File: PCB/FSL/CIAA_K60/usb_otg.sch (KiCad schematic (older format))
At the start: 13 parts, among them J502 USB OTG, U501 MIC2025-2YM, U502 PRTR5V0U2X

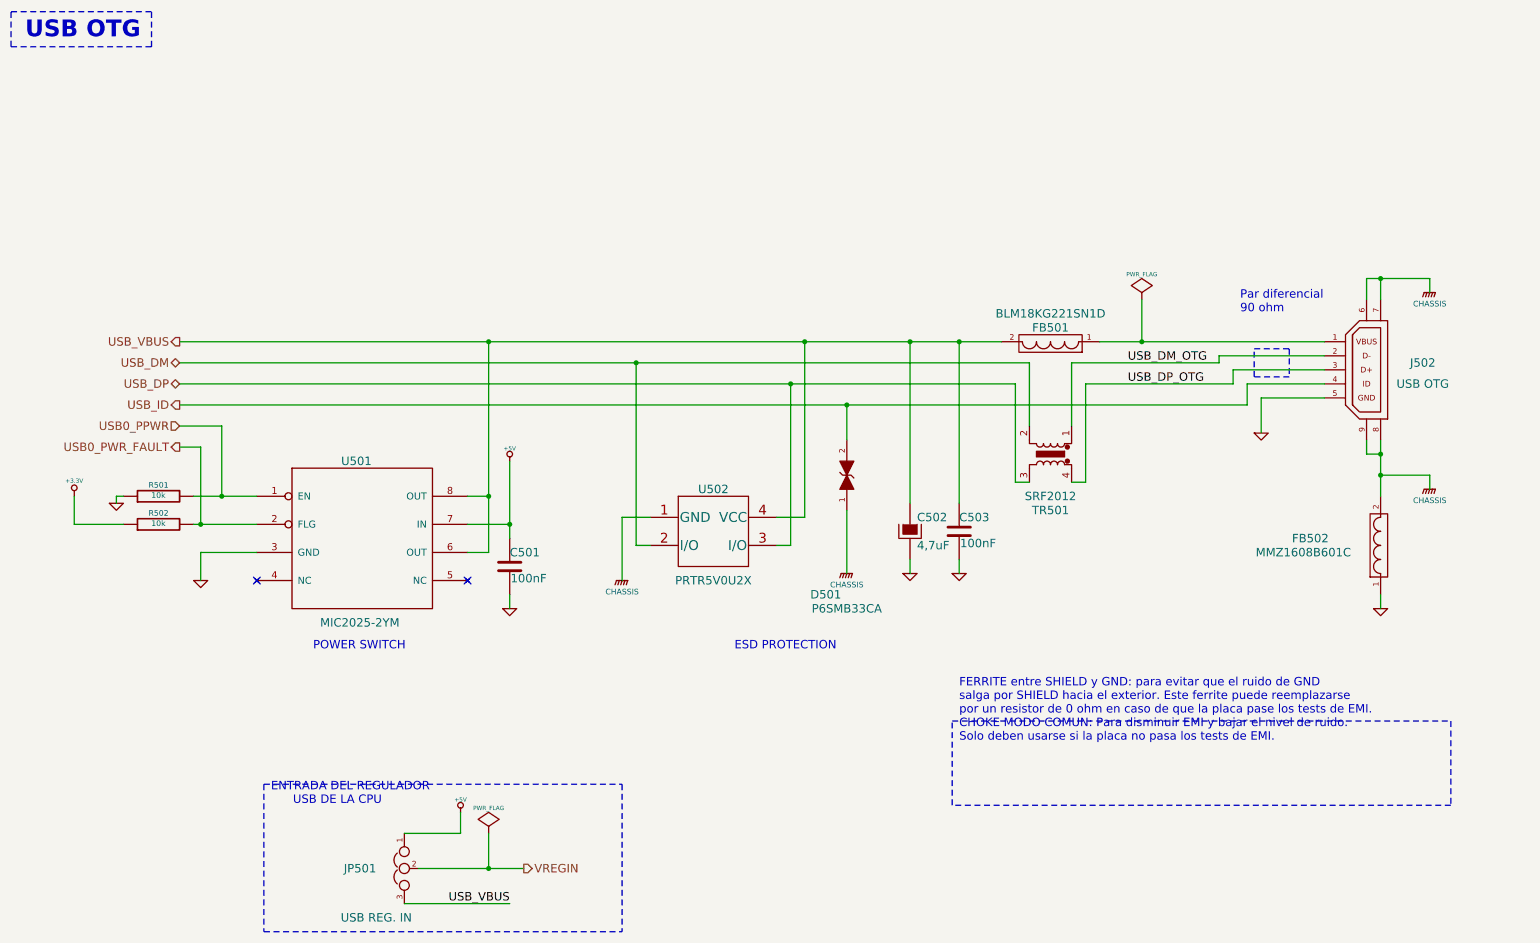
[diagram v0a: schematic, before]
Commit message: Actualizacion de esquematicos. Circuito impreso y modelos 3D
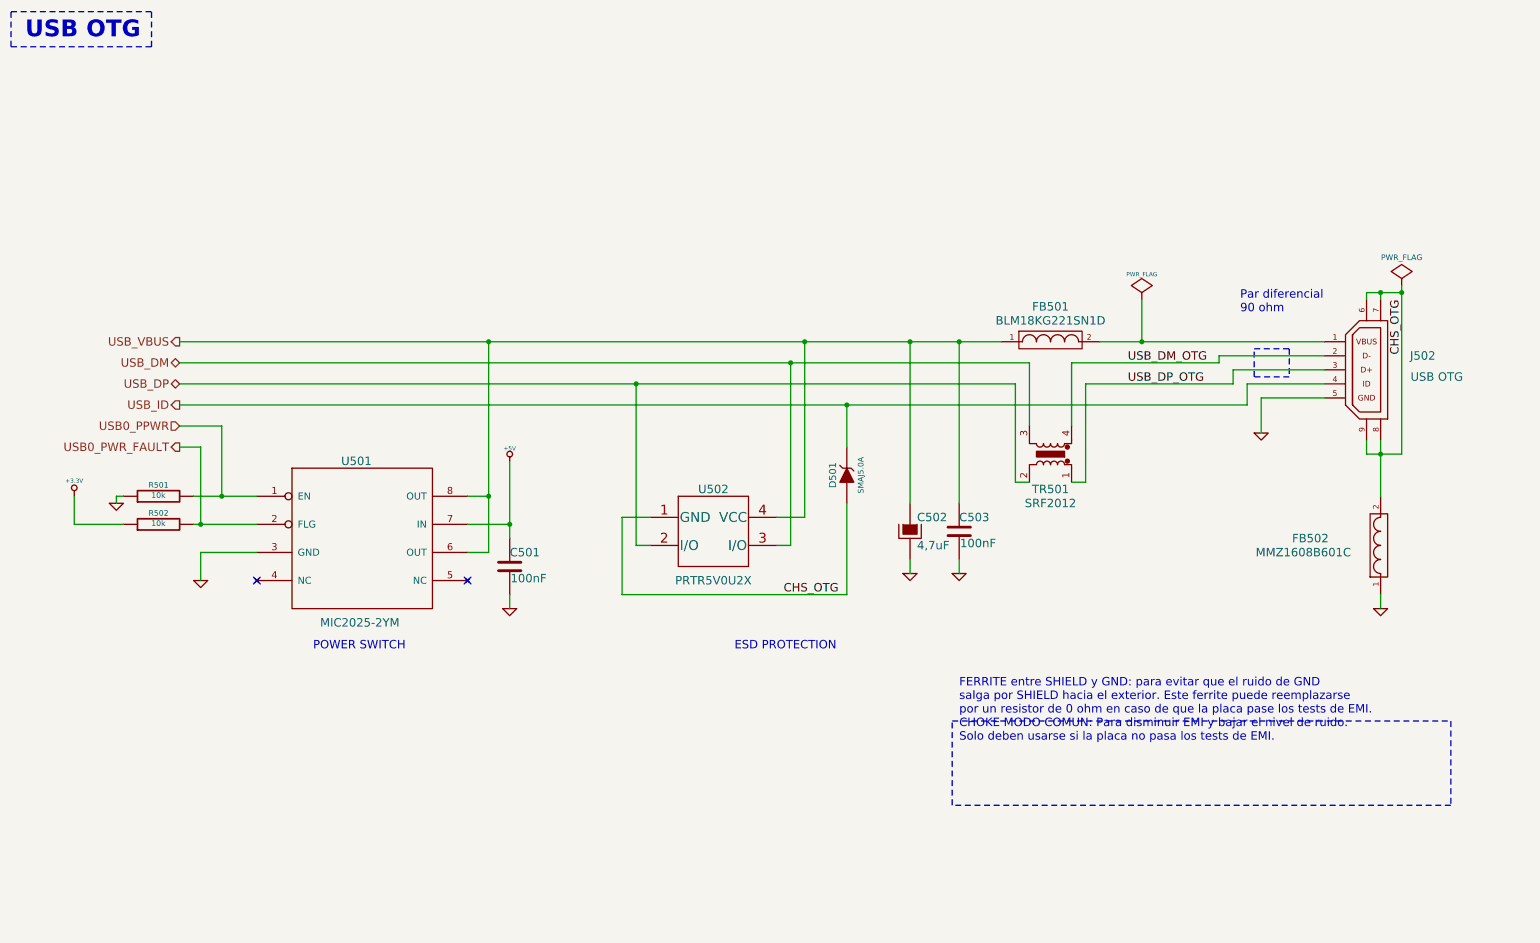
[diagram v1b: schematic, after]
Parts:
- removed D501: P6SMB33CA, DO-214AA_SMB, symbol TVS
- removed JP501: USB REG. IN, PIN_ARRAY_3x1, symbol JUMPER3
- added D501: SMAJ5.0A, DO-214AC_SMA, symbol ZENER
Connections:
- net USB_DM: now also TR501.3, U502.3 (I/O); no longer TR501.2, U502.2 (I/O)
- net USB_DM_OTG: now also TR501.4; no longer TR501.1
- net USB_DP: now also TR501.2, U502.2 (I/O); no longer TR501.3, U502.3 (I/O)
- net USB_DP_OTG: now also TR501.1; no longer TR501.4
- net USB_ID: now also D501.2 (K)
- net USB_VBUS: now also FB501.1; no longer FB501.2
- net at J502.1 (VBUS): now also FB501.2; no longer FB501.1
- net GNDPWR renamed CHS_OTG
- net CHS_OTG: now also D501.1 (A)
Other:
- note removed: "ENTRADA DEL REGULADOR\n USB DE LA CPU"

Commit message: Actualizacion de Licencia y avances
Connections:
- net USB_DM: now also U502.2 (I/O); no longer U502.3 (I/O)
- net USB_DP: now also U502.3 (I/O); no longer U502.2 (I/O)
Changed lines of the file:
@@
 Sheet 5 13
 Title "USB OTG"
-Date "24 jul 2014"
+Date "1 aug 2014"
 Rev "1.0"
 Comp "CIAA - COMPUTADORA INDUSTRIAL ABIERTA ARGENTINA. Versión FSL (Freescale K60)"
@@
 	6500 4700 4900 4700
 Wire Wire Line
-	5000 4350 5000 3200
-Connection ~ 5000 3200
-Wire Wire Line
-	6100 4350 6100 3050
-Connection ~ 6100 3050
+	6100 4350 6100 3200
+Connection ~ 6100 3200
+Wire Wire Line
+	5000 4350 5000 3050
+Connection ~ 5000 3050
 $EndSCHEMATC

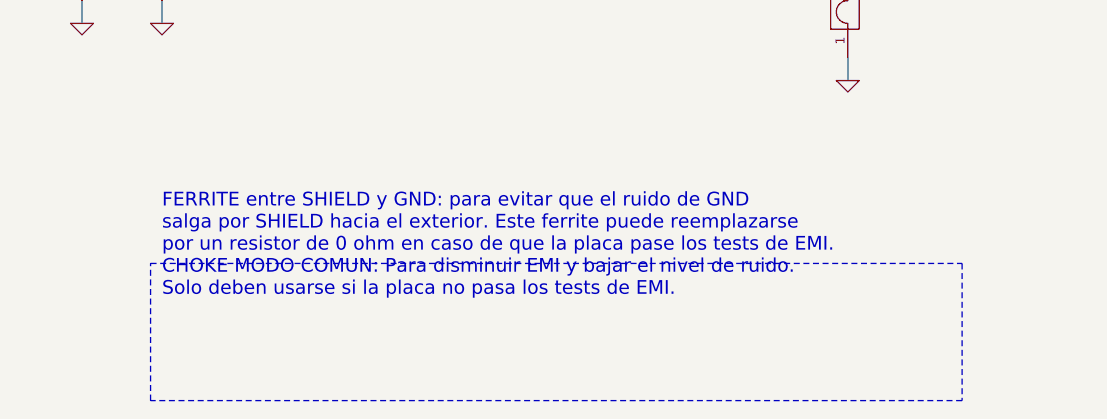
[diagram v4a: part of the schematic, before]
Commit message: Sch files adapted to new eeschema. Fixing some text locations.
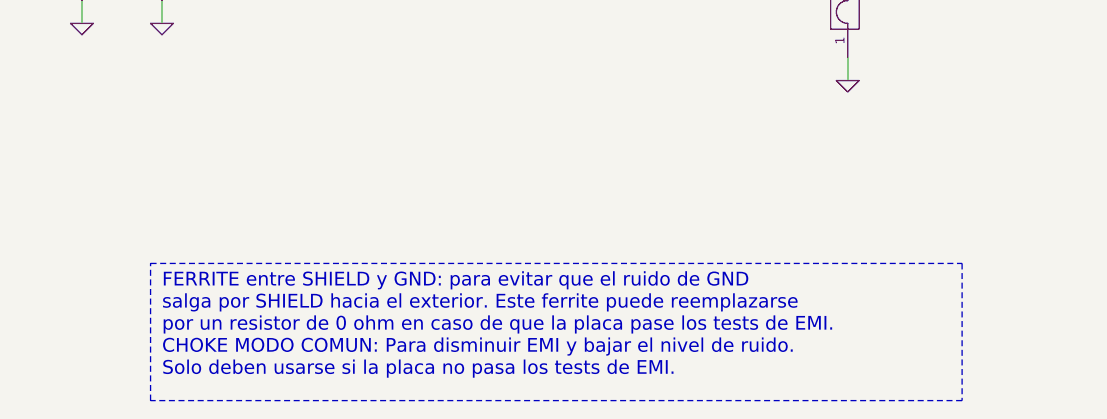
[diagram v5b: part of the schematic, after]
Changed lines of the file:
@@
 EESchema Schematic File Version 2
 LIBS:CIAAK60LIB
-EELAYER 27 0
+LIBS:CIAA_K60-cache
+EELAYER 25 0
 EELAYER END
 $Descr A4 11693 8268
@@
 Text Notes 9300 2700 0    60   ~ 0
 Par diferencial \n90 ohm
-Text Notes 7300 5750 0    60   ~ 0
+Text Notes 7300 6100 0    60   ~ 0
 FERRITE entre SHIELD y GND: para evitar que el ruido de GND\nsalga por SHIELD hacia el exterior. Este ferrite puede reemplazarse \npor un resistor de 0 ohm en caso de que la placa pase los tests de EMI. \nCHOKE MODO COMUN: Para disminuir EMI y bajar el nivel de ruido. \nSolo deben usarse si la placa no pasa los tests de EMI.
 Text Notes 2700 5100 0    60   ~ 0

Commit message: Renaming symbol field-names in .sch files for KiCost integration.
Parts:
- C501, C503: Desc (none) -> CAP CER 0,1UF 16V X7R 10% 0603; Descripcion CAP CER 0,1UF 16V X7R 10% 0603 -> (none); Digikey# (none) -> 399-1096-1-ND; Digikey/Mouser 399-1096-1-ND -> (none); Fabricante KEMET -> (none); Manf (none) -> Kemet; Manf# (none) -> C0603C104K4RACTU; Nro. parte C0603C104K4RACTU -> (none)
- C502: Desc (none) -> CAP TANT 4,7uF 6,3V 10% 1206; Descripcion CAP TANT 4,7uF 6,3V 10% 1206 -> (none); Digikey# (none) -> 399-9717-1-ND; Digikey/Mouser 399-9717-1-ND -> (none); Fabricante KEMET -> (none); Manf (none) -> Kemet; Manf# (none) -> T491A475K006AT; Nro. parte T491A475K006AT -> (none)
- D501: Desc (none) -> TVS DIODE 5VWM SMD; Descripcion TVS DIODE 5VWM SMD -> (none); Digikey# (none) -> SMAJ5.0ABCT-ND; Digikey/Mouser SMAJ5.0ABCT-ND -> (none); Fabricante Bourns Inc. -> (none); Manf (none) -> Bourns; Manf# (none) -> SMAJ5.0A; Nro. parte SMAJ5.0A -> (none)
- FB501: Desc (none) -> FERRITE CHIP 220 OHM 2200MA 0603; Descripcion FERRITE CHIP 220 OHM 2200MA 0603 -> (none); Digikey# (none) -> 490-5255-1-ND; Digikey/Mouser 490-5255-1-ND -> (none); Fabricante MURATA -> (none); Manf (none) -> MURATA; Manf# (none) -> BLM18KG221SN1D; Nro. parte BLM18KG221SN1D -> (none)
- FB502: Desc (none) -> FERRITE CHIP 600 OHM 500MA 0603; Descripcion FERRITE CHIP 600 OHM 500MA 0603 -> (none); Digikey# (none) -> 445-2166-1-ND; Digikey/Mouser 445-2166-1-ND -> (none); Fabricante TDK -> (none); Manf (none) -> TDK; Manf# (none) -> MMZ1608B601C; Nro. parte MMZ1608B601C -> (none)
- J502: Desc (none) -> CONNECTOR RECEPTACLE MICRO USB AB SMD BOTTOM MOUNT; Descripcion CONNECTOR RECEPTACLE MICRO USB AB SMD BOTTOM MOUNT -> (none); Digikey# (none) -> H11635TR-ND; Digikey/Mouser H11635TR-ND -> (none); Fabricante HIROSE ELECTRIC -> (none); Manf (none) -> HIROSE ELECTRIC; Manf# (none) -> ZX62-AB-5PA(11); Nro. parte ZX62-AB-5PA(11) -> (none)
- R501, R502: Desc (none) -> RESISTOR 10k 1/10W 5% 0603; Descripcion RESISTOR 10k 1/10W 5% 0603 -> (none); Digikey# (none) -> 311-10KGRCT-ND; Digikey/Mouser 311-10KGRCT-ND -> (none); Fabricante YAGEO -> (none); Manf (none) -> Yageo; Manf# (none) -> RC0603JR-0710KL; Nro. parte RC0603JR-0710KL -> (none)
- TR501: Desc (none) -> INDUCTOR COMMON MODE 90 OHM SMD; Descripcion INDUCTOR COMMON MODE 90 OHM SMD -> (none); Digikey# (none) -> SRF2012-900YCT-ND; Digikey/Mouser SRF2012-900YCT-ND -> (none); Fabricante BOURNS -> (none); Manf (none) -> BOURNS; Manf# (none) -> SRF2012-900Y; Nro. parte SRF2012-900Y -> (none)
- U501: Desc (none) -> IC SINGLE CHANNEL POWER DISTRIBUTION SWITCH 500mA; Descripcion IC SINGLE CHANNEL POWER DISTRIBUTION SWITCH 500mA -> (none); Digikey# (none) -> 576-1058-ND; Digikey/Mouser 576-1058-ND -> (none); Fabricante MICREL -> (none); Manf (none) -> MICREL; Manf# (none) -> MIC2025-2YM; Nro. parte MIC2025-2YM -> (none)
- U502: Desc (none) -> IC TVS DIODE 2 CHANNEL 10V CLAMP SOT1434; Descripcion IC TVS DIODE 2 CHANNEL 10V CLAMP SOT1434 -> (none); Digikey# (none) -> CM1213A-02SROSCT-ND; Digikey/Mouser CM1213A-02SROSCT-ND -> (none); Fabricante ON SEMICONDUCTOR -> (none); Manf (none) -> ON SEMICONDUCTOR; Manf# (none) -> CM1213A-02SR; Nro. parte CM1213A-02SR -> (none)
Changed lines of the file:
@@
 F 2 "SOIC-8" H 3050 4300 60  0001 C CNN
 F 3 "~" H 3050 4300 60  0000 C CNN
-F 4 "IC SINGLE CHANNEL POWER DISTRIBUTION SWITCH 500mA" H 3050 4300 60  0001 C CNN "Descripcion"
-F 5 "MICREL" H 3050 4300 60  0001 C CNN "Fabricante"
-F 6 "MIC2025-2YM" H 3050 4300 60  0001 C CNN "Nro. parte"
+F 4 "IC SINGLE CHANNEL POWER DISTRIBUTION SWITCH 500mA" H 3050 4300 60  0001 C CNN "Desc"
+F 5 "MICREL" H 3050 4300 60  0001 C CNN "Manf"
+F 6 "MIC2025-2YM" H 3050 4300 60  0001 C CNN "Manf#"
 F 7 "../datasheets/ic/mic2025.pdf" H 3050 4300 60  0001 C CNN "Path datasheet"
-F 8 "576-1058-ND" H 3050 4300 60  0001 C CNN "Digikey/Mouser"
+F 8 "576-1058-ND" H 3050 4300 60  0001 C CNN "Digikey#"
 F 9 "SOIC-8" H 3050 4300 60  0001 C CNN "Footprint estandar"
 	1    3050 4300
@@
 F 2 "SOT-143-4" H 7100 3600 60  0001 C CNN
 F 3 "~" H 7100 3600 60  0000 C CNN
-F 4 "IC TVS DIODE 2 CHANNEL 10V CLAMP SOT1434" H 5550 4250 60  0001 C CNN "Descripcion"
-F 5 "ON SEMICONDUCTOR" H 5550 4250 60  0001 C CNN "Fabricante"
-F 6 "CM1213A-02SR" H 5550 4250 60  0001 C CNN "Nro. parte"
+F 4 "IC TVS DIODE 2 CHANNEL 10V CLAMP SOT1434" H 5550 4250 60  0001 C CNN "Desc"
+F 5 "ON SEMICONDUCTOR" H 5550 4250 60  0001 C CNN "Manf"
+F 6 "CM1213A-02SR" H 5550 4250 60  0001 C CNN "Manf#"
 F 7 "../datasheets/passive/protect/CM1213A-D.PDF" H 5550 4250 60  0001 C CNN "Path datasheet"
-F 8 "CM1213A-02SROSCT-ND" H 5550 4250 60  0001 C CNN "Digikey/Mouser"
+F 8 "CM1213A-02SROSCT-ND" H 5550 4250 60  0001 C CNN "Digikey#"
 F 9 "SOT-143-4" H 5550 4250 60  0001 C CNN "Footprint estandar"
 	1    5550 4250
@@
 F 2 "c_1206POL" H 7050 4100 30  0001 C CNN
 F 3 "~" H 6950 4250 300 0000 C CNN
-F 4 "CAP TANT 4,7uF 6,3V 10% 1206 " H 6950 4250 60  0001 C CNN "Descripcion"
-F 5 "KEMET" H 6950 4250 60  0001 C CNN "Fabricante"
-F 6 "T491A475K006AT" H 6950 4250 60  0001 C CNN "Nro. parte"
+F 4 "CAP TANT 4,7uF 6,3V 10% 1206 " H 6950 4250 60  0001 C CNN "Desc"
+F 5 "Kemet" H 6950 4250 60  0001 C CNN "Manf"
+F 6 "T491A475K006AT" H 6950 4250 60  0001 C CNN "Manf#"
 F 7 "~" H 6950 4250 60  0001 C CNN "Path datasheet"
-F 8 "399-9717-1-ND" H 6950 4250 60  0001 C CNN "Digikey/Mouser"
+F 8 "399-9717-1-ND" H 6950 4250 60  0001 C CNN "Digikey#"
 F 9 "1206" H 6950 4250 60  0001 C CNN "Footprint estandar"
 	1    6950 4250
@@
 F 2 "c_0603" H 4138 4350 30  0001 C CNN
 F 3 "~" H 4100 4500 60  0000 C CNN
-F 4 "CAP CER 0,1UF 16V X7R 10% 0603" H 4100 4500 60  0001 C CNN "Descripcion"
-F 5 "KEMET" H 4100 4500 60  0001 C CNN "Fabricante"
-F 6 "C0603C104K4RACTU" H 4100 4500 60  0001 C CNN "Nro. parte"
+F 4 "CAP CER 0,1UF 16V X7R 10% 0603" H 4100 4500 60  0001 C CNN "Desc"
+F 5 "Kemet" H 4100 4500 60  0001 C CNN "Manf"
+F 6 "C0603C104K4RACTU" H 4100 4500 60  0001 C CNN "Manf#"
 F 7 "~" H 4100 4500 60  0001 C CNN "Path datasheet"
-F 8 "399-1096-1-ND" H 4100 4500 60  0001 C CNN "Digikey/Mouser"
+F 8 "399-1096-1-ND" H 4100 4500 60  0001 C CNN "Digikey#"
 F 9 "0603" H 4100 4500 60  0001 C CNN "Footprint estandar"
 	1    4100 4500
@@
 F 2 "fb_0603" H 10300 4350 60  0001 C CNN
 F 3 "~" H 10300 4350 60  0000 C CNN
-F 4 "FERRITE CHIP 600 OHM 500MA 0603" H 10300 4350 60  0001 C CNN "Descripcion"
-F 5 "TDK" H 10300 4350 60  0001 C CNN "Fabricante"
-F 6 "MMZ1608B601C" H 10300 4350 60  0001 C CNN "Nro. parte"
+F 4 "FERRITE CHIP 600 OHM 500MA 0603" H 10300 4350 60  0001 C CNN "Desc"
+F 5 "TDK" H 10300 4350 60  0001 C CNN "Manf"
+F 6 "MMZ1608B601C" H 10300 4350 60  0001 C CNN "Manf#"
 F 7 "../datasheets/passive/Ferrite/E9412_MMZ.pdf" H 10300 4350 60  0001 C CNN "Path datasheet"
-F 8 "445-2166-1-ND" H 10300 4350 60  0001 C CNN "Digikey/Mouser"
+F 8 "445-2166-1-ND" H 10300 4350 60  0001 C CNN "Digikey#"
 F 9 "0603" H 10300 4350 60  0001 C CNN "Footprint estandar"
 	1    10300 4350
@@
 F 2 "r_0603" V 1530 4200 30  0001 C CNN
 F 3 "~" H 1600 4200 30  0001 C CNN
-F 4 "RESISTOR 10k 1/10W 5% 0603 " H 1600 4200 60  0001 C CNN "Descripcion"
-F 5 "YAGEO" H 1600 4200 60  0001 C CNN "Fabricante"
-F 6 "RC0603JR-0710KL" H 1600 4200 60  0001 C CNN "Nro. parte"
+F 4 "RESISTOR 10k 1/10W 5% 0603 " H 1600 4200 60  0001 C CNN "Desc"
+F 5 "Yageo" H 1600 4200 60  0001 C CNN "Manf"
+F 6 "RC0603JR-0710KL" H 1600 4200 60  0001 C CNN "Manf#"
 F 7 "~" H 1600 4200 60  0001 C CNN "Path datasheet"
-F 8 "311-10KGRCT-ND" H 1600 4200 60  0001 C CNN "Digikey/Mouser"
+F 8 "311-10KGRCT-ND" H 1600 4200 60  0001 C CNN "Digikey#"
 F 9 "0603" H 1600 4200 60  0001 C CNN "Footprint estandar"
 	1    1600 4200
@@
 F 2 "r_0603" V 1530 4000 30  0001 C CNN
 F 3 "~" H 1600 4000 30  0001 C CNN
-F 4 "RESISTOR 10k 1/10W 5% 0603 " H 1600 4000 60  0001 C CNN "Descripcion"
-F 5 "YAGEO" H 1600 4000 60  0001 C CNN "Fabricante"
-F 6 "RC0603JR-0710KL" H 1600 4000 60  0001 C CNN "Nro. parte"
+F 4 "RESISTOR 10k 1/10W 5% 0603 " H 1600 4000 60  0001 C CNN "Desc"
+F 5 "Yageo" H 1600 4000 60  0001 C CNN "Manf"
+F 6 "RC0603JR-0710KL" H 1600 4000 60  0001 C CNN "Manf#"
 F 7 "~" H 1600 4000 60  0001 C CNN "Path datasheet"
-F 8 "311-10KGRCT-ND" H 1600 4000 60  0001 C CNN "Digikey/Mouser"
+F 8 "311-10KGRCT-ND" H 1600 4000 60  0001 C CNN "Digikey#"
 F 9 "0603" H 1600 4000 60  0001 C CNN "Footprint estandar"
 	1    1600 4000
@@
 F 2 "fb_0603" H 7950 2900 60  0001 C CNN
 F 3 "~" H 7950 2900 60  0000 C CNN
-F 4 "FERRITE CHIP 220 OHM 2200MA 0603" H 7950 2900 60  0001 C CNN "Descripcion"
-F 5 "MURATA" H 7950 2900 60  0001 C CNN "Fabricante"
-F 6 "BLM18KG221SN1D" H 7950 2900 60  0001 C CNN "Nro. parte"
+F 4 "FERRITE CHIP 220 OHM 2200MA 0603" H 7950 2900 60  0001 C CNN "Desc"
+F 5 "MURATA" H 7950 2900 60  0001 C CNN "Manf"
+F 6 "BLM18KG221SN1D" H 7950 2900 60  0001 C CNN "Manf#"
 F 7 "../datasheets/passive/Ferrite/L0110S0100BLM18K.pdf" H 7950 2900 60  0001 C CNN "Path datasheet"
-F 8 "490-5255-1-ND" H 7950 2900 60  0001 C CNN "Digikey/Mouser"
+F 8 "490-5255-1-ND" H 7950 2900 60  0001 C CNN "Digikey#"
 F 9 "0603" H 7950 2900 60  0001 C CNN "Footprint estandar"
 	1    7950 2900
@@
 F 2 "SRF2012" H 7950 3700 60  0001 C CNN
 F 3 "~" H 7950 3700 60  0000 C CNN
-F 4 "INDUCTOR COMMON MODE 90 OHM SMD" H 7950 3700 60  0001 C CNN "Descripcion"
-F 5 "BOURNS" H 7950 3700 60  0001 C CNN "Fabricante"
-F 6 "SRF2012-900Y" H 7950 3700 60  0001 C CNN "Nro. parte"
+F 4 "INDUCTOR COMMON MODE 90 OHM SMD" H 7950 3700 60  0001 C CNN "Desc"
+F 5 "BOURNS" H 7950 3700 60  0001 C CNN "Manf"
+F 6 "SRF2012-900Y" H 7950 3700 60  0001 C CNN "Manf#"
 F 7 "../datasheets/passive/inductor/SFR2012.pdf" H 7950 3700 60  0001 C CNN "Path datasheet"
-F 8 "SRF2012-900YCT-ND" H 7950 3700 60  0001 C CNN "Digikey/Mouser"
+F 8 "SRF2012-900YCT-ND" H 7950 3700 60  0001 C CNN "Digikey#"
 F 9 "~" H 7950 3700 60  0001 C CNN "Footprint estandar"
 	1    7950 3700
@@
 F 2 "c_0603" H 7338 4100 30  0001 C CNN
 F 3 "~" H 7300 4250 60  0000 C CNN
-F 4 "CAP CER 0,1UF 16V X7R 10% 0603" H 7300 4250 60  0001 C CNN "Descripcion"
-F 5 "KEMET" H 7300 4250 60  0001 C CNN "Fabricante"
-F 6 "C0603C104K4RACTU" H 7300 4250 60  0001 C CNN "Nro. parte"
+F 4 "CAP CER 0,1UF 16V X7R 10% 0603" H 7300 4250 60  0001 C CNN "Desc"
+F 5 "Kemet" H 7300 4250 60  0001 C CNN "Manf"
+F 6 "C0603C104K4RACTU" H 7300 4250 60  0001 C CNN "Manf#"
 F 7 "~" H 7300 4250 60  0001 C CNN "Path datasheet"
-F 8 "399-1096-1-ND" H 7300 4250 60  0001 C CNN "Digikey/Mouser"
+F 8 "399-1096-1-ND" H 7300 4250 60  0001 C CNN "Digikey#"
 F 9 "0603" H 7300 4250 60  0001 C CNN "Footprint estandar"
 	1    7300 4250
@@
 F 2 "DO-214AC_SMA" H 6500 3850 60  0001 C CNN
 F 3 "~" H 6500 3850 60  0000 C CNN
-F 4 "TVS DIODE 5VWM SMD" H 6500 3850 60  0001 C CNN "Descripcion"
-F 5 "Bourns Inc." H 6500 3850 60  0001 C CNN "Fabricante"
-F 6 "SMAJ5.0A" H 6500 3850 60  0001 C CNN "Nro. parte"
+F 4 "TVS DIODE 5VWM SMD" H 6500 3850 60  0001 C CNN "Desc"
+F 5 "Bourns" H 6500 3850 60  0001 C CNN "Manf"
+F 6 "SMAJ5.0A" H 6500 3850 60  0001 C CNN "Manf#"
 F 7 "../datasheets/passive/protect/SMAJ.pdf" H 6500 3850 60  0001 C CNN "Path datasheet"
-F 8 "SMAJ5.0ABCT-ND" H 6500 3850 60  0001 C CNN "Digikey/Mouser"
+F 8 "SMAJ5.0ABCT-ND" H 6500 3850 60  0001 C CNN "Digikey#"
 F 9 "SMA" H 6500 3850 60  0001 C CNN "Footprint estandar"
 	1    6500 3850
@@
 F 2 "USB_MicroAB" H 10550 3300 60  0001 C CNN
 F 3 "~" H 10650 3400 60  0000 C CNN
-F 4 "CONNECTOR RECEPTACLE MICRO USB AB SMD BOTTOM MOUNT" H 10800 3100 60  0001 C CNN "Descripcion"
-F 5 "HIROSE ELECTRIC" H 10850 3600 60  0001 C CNN "Fabricante"
-F 6 "ZX62-AB-5PA(11)" H 10950 3700 60  0001 C CNN "Nro. parte"
+F 4 "CONNECTOR RECEPTACLE MICRO USB AB SMD BOTTOM MOUNT" H 10800 3100 60  0001 C CNN "Desc"
+F 5 "HIROSE ELECTRIC" H 10850 3600 60  0001 C CNN "Manf"
+F 6 "ZX62-AB-5PA(11)" H 10950 3700 60  0001 C CNN "Manf#"
 F 7 "../datasheets/connectors/MICRO_USB_AB.pdf" H 11050 3800 60  0001 C CNN "Path datasheet"
-F 8 "H11635TR-ND" H 11150 3900 60  0001 C CNN "Digikey/Mouser"
+F 8 "H11635TR-ND" H 11150 3900 60  0001 C CNN "Digikey#"
 F 9 "~" H 11250 4000 60  0001 C CNN "Footprint estandar"
 	1    10350 3450
